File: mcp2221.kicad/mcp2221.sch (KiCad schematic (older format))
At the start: 17 parts, among them J2 Jumper 32 or 21, J3 Conn_01x04_Male, J4 Conn_01x07_Male, J5 Conn_01x02_Male, J6 Conn_01x02_Male, U1 AMS1117CD-3.3, U2 MCP2221

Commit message: replaced 4-pin USB-connector with 5-pin connector
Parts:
- removed USB1: Conn_01x04, symbol Connector_Generic:Conn_01x04
- added USB1: Micro-USB_Breakout, symbol User:Micro-USB_Breakout
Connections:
- wire segments 37 -> 41
- no-connect marks 0 -> 1
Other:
- note removed: "VBUS\nD+\nD-\nGND"
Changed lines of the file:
@@
 Sheet 1 1
 Title "MCP2221 Breakout"
-Date "2020-03-06"
-Rev "2"
+Date "2020-03-10"
+Rev "3"
 Comp "https://github.com/bablokb/pcb-mcp2221"
 Comment1 ""
@@
 L power:GND #PWR0102
 U 1 1 5E4BC7DA
-P 2300 2500
-F 0 "#PWR0102" H 2300 2250 50  0001 C CNN
-F 1 "GND" H 2305 2327 50  0000 C CNN
-F 2 "" H 2300 2500 50  0001 C CNN
-F 3 "" H 2300 2500 50  0001 C CNN
-	1    2300 2500
+P 3050 2600
+F 0 "#PWR0102" H 3050 2350 50  0001 C CNN
+F 1 "GND" H 3055 2427 50  0000 C CNN
+F 2 "" H 3050 2600 50  0001 C CNN
+F 3 "" H 3050 2600 50  0001 C CNN
+	1    3050 2600
 	1    0    0    -1
 $EndComp
@@
 	4200 2600 4200 2800
 Connection ~ 4200 2800
-$Comp
-L Connector_Generic:Conn_01x04 USB1
-U 1 1 5E611DD7
-P 2100 2400
-F 0 "USB1" H 2018 1975 50  0000 C CNN
-F 1 "Conn_01x04" H 2018 2066 50  0000 C CNN
-F 2 "" H 2100 2400 50  0001 C CNN
-F 3 "~" H 2100 2400 50  0001 C CNN
-	1    2100 2400
-	-1   0    0    1
-$EndComp
-Text Notes 2000 2500 2    50   ~ 0
-VBUS\nD+\nD-\nGND
-$Comp
-L power:PWR_FLAG #FLG0102
-U 1 1 5E615FD4
-P 2300 2500
-F 0 "#FLG0102" H 2300 2575 50  0001 C CNN
-F 1 "PWR_FLAG" V 2300 2627 50  0000 L CNN
-F 2 "" H 2300 2500 50  0001 C CNN
-F 3 "~" H 2300 2500 50  0001 C CNN
-	1    2300 2500
-	0    1    1    0
-$EndComp
-Connection ~ 2300 2500
 Wire Wire Line
 	2300 2200 2300 1800
@@
 Wire Wire Line
 	3500 2200 3500 2100
-Connection ~ 2300 2200
 $Comp
 L power:PWR_FLAG #FLG0103
@@
 Wire Wire Line
 	4000 2450 3850 2450
-$Comp
-L power:GND #PWR0106
-U 1 1 5E625316
-P 3550 2450
-F 0 "#PWR0106" H 3550 2200 50  0001 C CNN
-F 1 "GND" V 3555 2322 50  0000 R CNN
-F 2 "" H 3550 2450 50  0001 C CNN
-F 3 "" H 3550 2450 50  0001 C CNN
-	1    3550 2450
-	0    1    1    0
-$EndComp
 Connection ~ 3850 1450
 Wire Wire Line
@@
 Text Label 7250 1950 0    50   ~ 0
 ~RST~
+$Comp
+L User:Micro-USB_Breakout USB1
+U 1 1 5E68A411
+P 2100 2400
+F 0 "USB1" H 2100 2750 50  0000 C CNN
+F 1 "Micro-USB_Breakout" H 2100 2850 50  0000 C CNN
+F 2 "" H 2100 2400 50  0001 C CNN
+F 3 "~" H 2100 2400 50  0001 C CNN
+	1    2100 2400
+	-1   0    0    1
+$EndComp
+Connection ~ 2300 2200
+NoConn ~ 2300 2500
+Wire Wire Line
+	2300 2600 2750 2600
+Wire Wire Line
+	3550 2450 3050 2450
+Wire Wire Line
+	3050 2450 3050 2600
+Connection ~ 3050 2600
+$Comp
+L power:PWR_FLAG #FLG0102
+U 1 1 5E691293
+P 2750 2600
+F 0 "#FLG0102" H 2750 2675 50  0001 C CNN
+F 1 "PWR_FLAG" H 2550 2550 50  0000 L CNN
+F 2 "" H 2750 2600 50  0001 C CNN
+F 3 "~" H 2750 2600 50  0001 C CNN
+	1    2750 2600
+	-1   0    0    1
+$EndComp
+Connection ~ 2750 2600
+Wire Wire Line
+	2750 2600 3050 2600
+Text Label 5500 2300 0    50   ~ 0
+~RST~
 $EndSCHEMATC

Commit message: Rev 4: added pullups for all GPs, added SW1 to GP3
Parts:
- added J3, J4: Conn_01x02_Male, symbol Connector:Conn_01x02_Male
- added R4, R6: 2.2K, symbol Device:R
- added R5, R7: 2.2k, symbol Device:R
- added SW1: SW_Push, symbol Switch:SW_Push
- J6: renamed from J5; value Conn_01x02_Male -> Conn_01x03_Male; symbol Connector:Conn_01x02_Male -> Connector:Conn_01x03_Male
- J7: renamed from J6; value Conn_01x02_Male -> Conn_01x03_Male; symbol Connector:Conn_01x02_Male -> Connector:Conn_01x03_Male
- renumbered J4 to J1, J3 to J5, R5 to R1, R1 to R2, R2 to R3, R3 to R8, R4 to R9
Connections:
- net GND: now also SW1.2
- net GP0: now also J6.2 (Pin_2); no longer J6.1 (Pin_1)
- net GP2: now also J3.1 (Pin_1)
- net GP3: now also J4.2 (Pin_2), SW1.1
- net VDD: now reaches C2.1, J2.2 (Pin_2), J5.2 (Pin_2), R1.2, R2.1, R3.1, U2.1 (VDD)
- net VDD: now also R4.1, R5.2, R6.1, R7.2
- net at R8.1: now also J6.3 (Pin_3); no longer J6.2 (Pin_2)
- new net: J6.1 (Pin_1), R6.2
- new net: J7.3 (Pin_3), R7.1
- new net: J3.2 (Pin_2), R4.2
- new net: J4.1 (Pin_1), R5.1
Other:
- moved on the sheet: D1, D2, J1, R1, R8, R9

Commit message: added footprints, created initial pcb
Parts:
- C1, C2: footprint (none) -> Capacitor_THT:C_Disc_D4.3mm_W1.9mm_P5.00mm
- D1, D2: footprint (none) -> LED_THT:LED_Rectangular_W3.0mm_H2.0mm
- J1: footprint (none) -> Connector_PinHeader_2.54mm:PinHeader_1x07_P2.54mm_Vertical
- J2, J6, J7: footprint (none) -> Connector_PinHeader_2.54mm:PinHeader_1x03_P2.54mm_Vertical
- J3, J4: footprint (none) -> Connector_PinHeader_2.54mm:PinHeader_1x02_P2.54mm_Vertical
- J5: footprint (none) -> Connector_PinHeader_2.54mm:PinHeader_1x04_P2.54mm_Vertical
- R1, R2, R3, R4, R5, R6, R7, R8, R9: footprint (none) -> Resistor_THT:R_Axial_DIN0204_L3.6mm_D1.6mm_P7.62mm_Horizontal
- SW1: footprint (none) -> Button_Switch_THT:SW_DIP_SPSTx01_Piano_10.8x4.1mm_W7.62mm_P2.54mm
- U1: footprint Package_TO_SOT_SMD:TO-252-3_TabPin2 -> user:AMS1117_Breakout
- USB1: footprint (none) -> user:Micro-USB_Breakout
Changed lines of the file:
@@
 F 0 "U1" H 3150 1692 50  0000 C CNN
 F 1 "AMS1117CD-3.3" H 3150 1601 50  0000 C CNN
-F 2 "Package_TO_SOT_SMD:TO-252-3_TabPin2" H 3150 1650 50  0001 C CNN
+F 2 "user:AMS1117_Breakout" H 3150 1650 50  0001 C CNN
 F 3 "http://www.advanced-monolithic.com/pdf/ds1117.pdf" H 3250 1200 50  0001 C CNN
 	1    3150 1450
@@
 F 0 "J5" H 5072 3482 50  0000 R CNN
 F 1 "Conn_01x04_Male" H 5072 3573 50  0000 R CNN
-F 2 "" H 5100 3600 50  0001 C CNN
+F 2 "Connector_PinHeader_2.54mm:PinHeader_1x04_P2.54mm_Vertical" H 5100 3600 50  0001 C CNN
 F 3 "~" H 5100 3600 50  0001 C CNN
 	1    5100 3600
@@
 F 0 "R2" H 4270 3196 50  0000 L CNN
 F 1 "2.2k" H 4270 3105 50  0000 L CNN
-F 2 "" V 4130 3150 50  0001 C CNN
+F 2 "Resistor_THT:R_Axial_DIN0204_L3.6mm_D1.6mm_P7.62mm_Horizontal" V 4130 3150 50  0001 C CNN
 F 3 "~" H 4200 3150 50  0001 C CNN
 	1    4200 3150
@@
 F 0 "R3" H 4520 3196 50  0000 L CNN
 F 1 "2.2K" H 4520 3105 50  0000 L CNN
-F 2 "" V 4380 3150 50  0001 C CNN
+F 2 "Resistor_THT:R_Axial_DIN0204_L3.6mm_D1.6mm_P7.62mm_Horizontal" V 4380 3150 50  0001 C CNN
 F 3 "~" H 4450 3150 50  0001 C CNN
 	1    4450 3150
@@
 F 0 "R8" H 6450 4100 50  0000 L CNN
 F 1 "1K" H 6450 4000 50  0000 L CNN
-F 2 "" V 6580 4050 50  0001 C CNN
+F 2 "Resistor_THT:R_Axial_DIN0204_L3.6mm_D1.6mm_P7.62mm_Horizontal" V 6580 4050 50  0001 C CNN
 F 3 "~" H 6650 4050 50  0001 C CNN
 	1    6650 4050
@@
 F 0 "R9" H 6970 4096 50  0000 L CNN
 F 1 "1K" H 6970 4005 50  0000 L CNN
-F 2 "" V 6830 4050 50  0001 C CNN
+F 2 "Resistor_THT:R_Axial_DIN0204_L3.6mm_D1.6mm_P7.62mm_Horizontal" V 6830 4050 50  0001 C CNN
 F 3 "~" H 6900 4050 50  0001 C CNN
 	1    6900 4050
@@
 F 0 "D1" V 6700 4550 50  0000 R CNN
 F 1 "LED" V 6600 4600 50  0000 R CNN
-F 2 "" H 6650 4350 50  0001 C CNN
+F 2 "LED_THT:LED_Rectangular_W3.0mm_H2.0mm" H 6650 4350 50  0001 C CNN
 F 3 "~" H 6650 4350 50  0001 C CNN
 	1    6650 4350
@@
 F 0 "D2" V 6939 4233 50  0000 R CNN
 F 1 "LED" V 6848 4233 50  0000 R CNN
-F 2 "" H 6900 4350 50  0001 C CNN
+F 2 "LED_THT:LED_Rectangular_W3.0mm_H2.0mm" H 6900 4350 50  0001 C CNN
 F 3 "~" H 6900 4350 50  0001 C CNN
 	1    6900 4350
@@
 F 0 "J6" H 6300 3800 50  0000 C CNN
 F 1 "Conn_01x03_Male" H 6100 3700 50  0000 C CNN
-F 2 "" H 6450 3800 50  0001 C CNN
+F 2 "Connector_PinHeader_2.54mm:PinHeader_1x03_P2.54mm_Vertical" H 6450 3800 50  0001 C CNN
 F 3 "~" H 6450 3800 50  0001 C CNN
 	1    6450 3800
@@
 F 0 "J7" H 7072 3682 50  0000 R CNN
 F 1 "Conn_01x03_Male" H 7072 3773 50  0000 R CNN
-F 2 "" H 7100 3800 50  0001 C CNN
+F 2 "Connector_PinHeader_2.54mm:PinHeader_1x03_P2.54mm_Vertical" H 7100 3800 50  0001 C CNN
 F 3 "~" H 7100 3800 50  0001 C CNN
 	1    7100 3800
@@
 F 0 "C1" H 3600 1000 50  0000 C CNN
 F 1 "0.47µF" H 3550 1100 50  0000 C CNN
-F 2 "" H 3888 900 50  0001 C CNN
+F 2 "Capacitor_THT:C_Disc_D4.3mm_W1.9mm_P5.00mm" H 3888 900 50  0001 C CNN
 F 3 "~" H 3850 1050 50  0001 C CNN
 	1    3850 1050
@@
 F 0 "J2" V 3662 2044 50  0000 L CNN
 F 1 "Jumper 32 or 21" V 3550 1700 50  0000 L CNN
-F 2 "" H 3600 1900 50  0001 C CNN
+F 2 "Connector_PinHeader_2.54mm:PinHeader_1x03_P2.54mm_Vertical" H 3600 1900 50  0001 C CNN
 F 3 "~" H 3600 1900 50  0001 C CNN
 	1    3600 1900
@@
 F 0 "R1" H 5570 2596 50  0000 L CNN
 F 1 "10K" H 5570 2505 50  0000 L CNN
-F 2 "" V 5430 2550 50  0001 C CNN
+F 2 "Resistor_THT:R_Axial_DIN0204_L3.6mm_D1.6mm_P7.62mm_Horizontal" V 5430 2550 50  0001 C CNN
 F 3 "~" H 5500 2550 50  0001 C CNN
 	1    5500 2550
@@
 F 0 "C2" V 3850 2450 50  0000 C CNN
 F 1 "0.1 µF" V 3950 2450 50  0000 C CNN
-F 2 "" H 3738 2300 50  0001 C CNN
+F 2 "Capacitor_THT:C_Disc_D4.3mm_W1.9mm_P5.00mm" H 3738 2300 50  0001 C CNN
 F 3 "~" H 3700 2450 50  0001 C CNN
 	1    3700 2450
@@
 F 0 "USB1" H 2100 2750 50  0000 C CNN
 F 1 "Micro-USB_Breakout" H 2100 2850 50  0000 C CNN
-F 2 "" H 2100 2400 50  0001 C CNN
+F 2 "user:Micro-USB_Breakout" H 2100 2400 50  0001 C CNN
 F 3 "~" H 2100 2400 50  0001 C CNN
 	1    2100 2400
@@
 F 0 "R6" H 6570 3496 50  0000 L CNN
 F 1 "2.2K" H 6570 3405 50  0000 L CNN
-F 2 "" V 6430 3450 50  0001 C CNN
+F 2 "Resistor_THT:R_Axial_DIN0204_L3.6mm_D1.6mm_P7.62mm_Horizontal" V 6430 3450 50  0001 C CNN
 F 3 "~" H 6500 3450 50  0001 C CNN
 	1    6500 3450
@@
 F 0 "R7" H 7120 3496 50  0000 L CNN
 F 1 "2.2k" H 7120 3405 50  0000 L CNN
-F 2 "" V 6980 3450 50  0001 C CNN
+F 2 "Resistor_THT:R_Axial_DIN0204_L3.6mm_D1.6mm_P7.62mm_Horizontal" V 6980 3450 50  0001 C CNN
 F 3 "~" H 7050 3450 50  0001 C CNN
 	1    7050 3450
@@
 F 0 "R4" H 8470 3446 50  0000 L CNN
 F 1 "2.2K" H 8470 3355 50  0000 L CNN
-F 2 "" V 8330 3400 50  0001 C CNN
+F 2 "Resistor_THT:R_Axial_DIN0204_L3.6mm_D1.6mm_P7.62mm_Horizontal" V 8330 3400 50  0001 C CNN
 F 3 "~" H 8400 3400 50  0001 C CNN
 	1    8400 3400
@@
 F 0 "R5" H 9020 3446 50  0000 L CNN
 F 1 "2.2k" H 9020 3355 50  0000 L CNN
-F 2 "" V 8880 3400 50  0001 C CNN
+F 2 "Resistor_THT:R_Axial_DIN0204_L3.6mm_D1.6mm_P7.62mm_Horizontal" V 8880 3400 50  0001 C CNN
 F 3 "~" H 8950 3400 50  0001 C CNN
 	1    8950 3400
@@
 F 0 "J3" H 8250 2950 50  0000 C CNN
 F 1 "Conn_01x02_Male" H 7950 2850 50  0000 C CNN
-F 2 "" H 8350 2950 50  0001 C CNN
+F 2 "Connector_PinHeader_2.54mm:PinHeader_1x02_P2.54mm_Vertical" H 8350 2950 50  0001 C CNN
 F 3 "~" H 8350 2950 50  0001 C CNN
 	1    8350 2950
@@
 F 0 "J4" H 8972 2932 50  0000 R CNN
 F 1 "Conn_01x02_Male" H 8972 3023 50  0000 R CNN
-F 2 "" H 9000 3050 50  0001 C CNN
+F 2 "Connector_PinHeader_2.54mm:PinHeader_1x02_P2.54mm_Vertical" H 9000 3050 50  0001 C CNN
 F 3 "~" H 9000 3050 50  0001 C CNN
 	1    9000 3050
@@
 F 0 "J1" V 7600 1750 50  0000 C CNN
 F 1 "Conn_01x07_Male" V 7450 1800 50  0000 C CNN
-F 2 "" H 7000 1750 50  0001 C CNN
+F 2 "Connector_PinHeader_2.54mm:PinHeader_1x07_P2.54mm_Vertical" H 7000 1750 50  0001 C CNN
 F 3 "~" H 7000 1750 50  0001 C CNN
 	1    7000 1750
@@
 F 0 "SW1" H 8150 2535 50  0000 C CNN
 F 1 "SW_Push" H 8150 2444 50  0000 C CNN
-F 2 "" H 8150 2450 50  0001 C CNN
+F 2 "Button_Switch_THT:SW_DIP_SPSTx01_Piano_10.8x4.1mm_W7.62mm_P2.54mm" H 8150 2450 50  0001 C CNN
 F 3 "~" H 8150 2450 50  0001 C CNN
 	1    8150 2250
@@
 	7950 2500 8800 2500
 $Comp
-L power:GND #PWR?
+L power:GND #PWR0101
 U 1 1 5E6B663C
 P 8550 2250
-F 0 "#PWR?" H 8550 2000 50  0001 C CNN
+F 0 "#PWR0101" H 8550 2000 50  0001 C CNN
 F 1 "GND" H 8555 2077 50  0000 C CNN
 F 2 "" H 8550 2250 50  0001 C CNN

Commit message: Rev 6: switched to SMD, added connector, minor tweaks
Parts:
- added J6: Conn_01x06_Male, Connector_PinHeader_2.54mm:PinHeader_1x06_P2.54mm_Vertical, symbol Connector:Conn_01x06_Male
- C1: renamed from C2; footprint Capacitor_THT:C_Disc_D4.3mm_W1.9mm_P5.00mm -> Capacitor_SMD:C_1206_3216Metric_Pad1.42x1.75mm_HandSolder
- C2: renamed from C1; footprint Capacitor_THT:C_Disc_D4.3mm_W1.9mm_P5.00mm -> Capacitor_SMD:C_1206_3216Metric_Pad1.42x1.75mm_HandSolder
- D1, D2: footprint LED_THT:LED_Rectangular_W3.0mm_H2.0mm -> LED_SMD:LED_1206_3216Metric_Pad1.42x1.75mm_HandSolder
- J4: renamed from J1; value Conn_01x07_Male -> Conn_01x06_Male; footprint Connector_PinHeader_2.54mm:PinHeader_1x07_P2.54mm_Vertical -> Connector_PinHeader_2.54mm:PinHeader_1x06_P2.54mm_Vertical; symbol Connector:Conn_01x07_Male -> Connector:Conn_01x06_Male
- R1: renamed from R2; footprint Resistor_THT:R_Axial_DIN0204_L3.6mm_D1.6mm_P7.62mm_Horizontal -> Resistor_SMD:R_1206_3216Metric_Pad1.42x1.75mm_HandSolder
- R2: renamed from R3; footprint Resistor_THT:R_Axial_DIN0204_L3.6mm_D1.6mm_P7.62mm_Horizontal -> Resistor_SMD:R_1206_3216Metric_Pad1.42x1.75mm_HandSolder
- R3: renamed from R1; footprint Resistor_THT:R_Axial_DIN0204_L3.6mm_D1.6mm_P7.62mm_Horizontal -> Resistor_SMD:R_1206_3216Metric_Pad1.42x1.75mm_HandSolder
- R4: renamed from R6; value 2.2K -> 4.7K; footprint Resistor_THT:R_Axial_DIN0204_L3.6mm_D1.6mm_P7.62mm_Horizontal -> Resistor_SMD:R_1206_3216Metric_Pad1.42x1.75mm_HandSolder
- R5: renamed from R8; footprint Resistor_THT:R_Axial_DIN0204_L3.6mm_D1.6mm_P7.62mm_Horizontal -> Resistor_SMD:R_1206_3216Metric_Pad1.42x1.75mm_HandSolder
- R6: renamed from R9; footprint Resistor_THT:R_Axial_DIN0204_L3.6mm_D1.6mm_P7.62mm_Horizontal -> Resistor_SMD:R_1206_3216Metric_Pad1.42x1.75mm_HandSolder
- R7: value 2.2k -> 4.7K; footprint Resistor_THT:R_Axial_DIN0204_L3.6mm_D1.6mm_P7.62mm_Horizontal -> Resistor_SMD:R_1206_3216Metric_Pad1.42x1.75mm_HandSolder
- R8: renamed from R4; value 2.2K -> 4.7K; footprint Resistor_THT:R_Axial_DIN0204_L3.6mm_D1.6mm_P7.62mm_Horizontal -> Resistor_SMD:R_1206_3216Metric_Pad1.42x1.75mm_HandSolder
- R9: renamed from R5; value 2.2k -> 4.7K; footprint Resistor_THT:R_Axial_DIN0204_L3.6mm_D1.6mm_P7.62mm_Horizontal -> Resistor_SMD:R_1206_3216Metric_Pad1.42x1.75mm_HandSolder
- SW1: footprint Button_Switch_THT:SW_DIP_SPSTx01_Piano_10.8x4.1mm_W7.62mm_P2.54mm -> Button_Switch_SMD:SW_Push_1P1T_NO_6x6mm_H9.5mm
- renumbered J2 to J1, J5 to J2, J6 to J3, J7 to J5, J3 to J7, J4 to J8
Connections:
- net GND: now also J6.5 (Pin_5)
- net GP3: now also J8.1 (Pin_1); no longer J8.2 (Pin_2)
- net SCL: now also J6.2 (Pin_2)
- net SDA: now also J6.1 (Pin_1)
- net ~RST~: now also J6.3 (Pin_3); no longer J4.7 (Pin_7)
- net 3.3V: now reaches C2.1, J1.1 (Pin_1), U1.2 (VO), U2.11 (VUSB)
- net 3.3V: now also J6.4 (Pin_4)
- net 5V: now reaches J1.3 (Pin_3), U1.3 (VI), USB1.5 (Pin_5)
- net 5V: now also J6.6 (Pin_6)
- net at R6.1: now also J5.3 (Pin_3); no longer J5.1 (Pin_1)
- net at R7.1: now also J5.1 (Pin_1); no longer J5.3 (Pin_3)
- net at R9.1: now also J8.2 (Pin_2); no longer J8.1 (Pin_1)

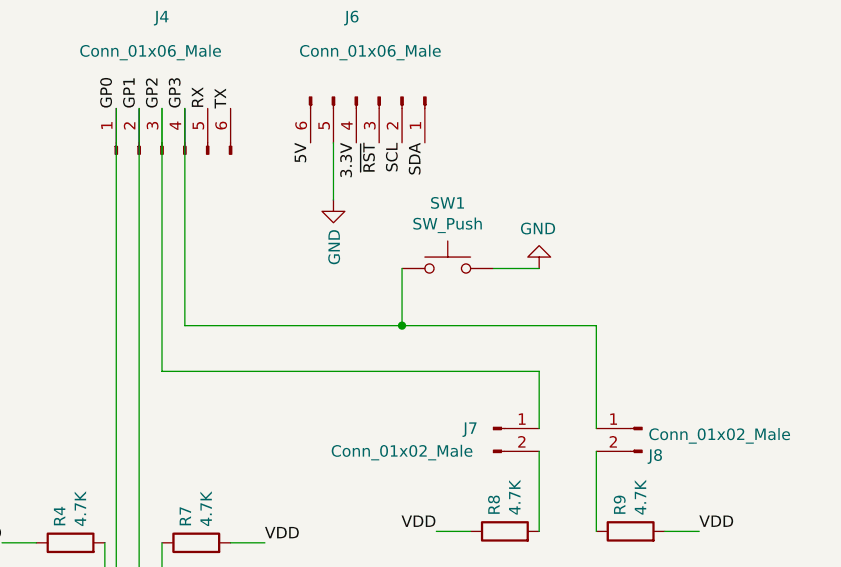
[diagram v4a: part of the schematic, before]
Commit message: Rev 7: added button for GP2
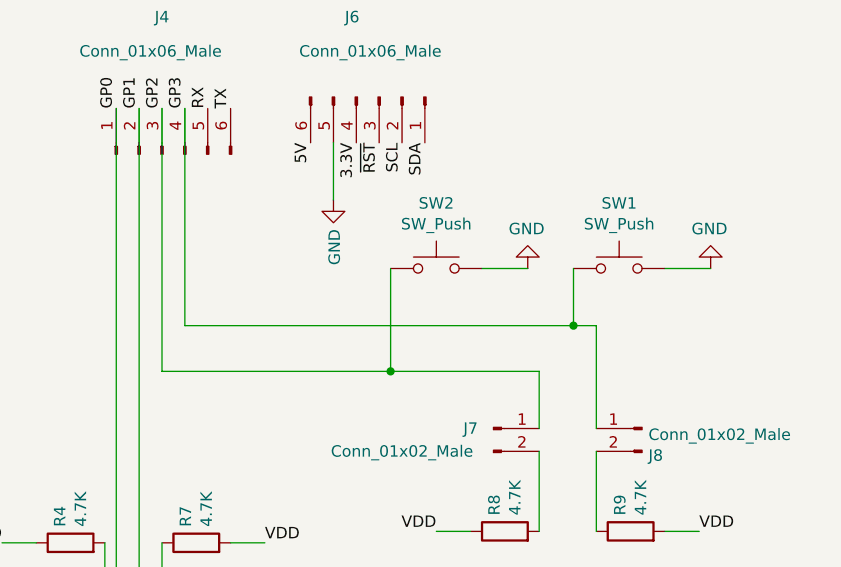
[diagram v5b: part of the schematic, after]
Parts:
- added SW2: SW_Push, Button_Switch_SMD:SW_Push_1P1T_NO_6x6mm_H9.5mm, symbol Switch:SW_Push
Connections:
- net GND: now also SW2.2
- net GP2: now also SW2.1
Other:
- moved on the sheet: SW1
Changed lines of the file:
@@
 Sheet 1 1
 Title "MCP2221 Breakout"
-Date "2020-04-09"
-Rev "6"
+Date "2020-04-14"
+Rev "7"
 Comp "https://github.com/bablokb/pcb-mcp2221"
 Comment1 ""
@@
 	8550 3050 8550 3400
 Wire Wire Line
-	6900 2700 8550 2700
+	6900 2700 7900 2700
 Wire Wire Line
 	8550 2700 8550 2950
-Wire Wire Line
-	7000 2500 7950 2500
 Wire Wire Line
 	8800 2500 8800 2950
@@
 L Switch:SW_Push SW1
 U 1 1 5E6B4B53
-P 8150 2250
-F 0 "SW1" H 8150 2535 50  0000 C CNN
-F 1 "SW_Push" H 8150 2444 50  0000 C CNN
-F 2 "Button_Switch_SMD:SW_Push_1P1T_NO_6x6mm_H9.5mm" H 8150 2450 50  0001 C CNN
-F 3 "~" H 8150 2450 50  0001 C CNN
-	1    8150 2250
-	1    0    0    -1
-$EndComp
-Wire Wire Line
-	7950 2250 7950 2500
-Connection ~ 7950 2500
-Wire Wire Line
-	7950 2500 8800 2500
+P 8900 2250
+F 0 "SW1" H 8900 2535 50  0000 C CNN
+F 1 "SW_Push" H 8900 2444 50  0000 C CNN
+F 2 "Button_Switch_SMD:SW_Push_1P1T_NO_6x6mm_H9.5mm" H 8900 2450 50  0001 C CNN
+F 3 "~" H 8900 2450 50  0001 C CNN
+	1    8900 2250
+	1    0    0    -1
+$EndComp
+Wire Wire Line
+	8700 2250 8700 2500
 $Comp
 L power:GND #PWR09
 U 1 1 5E6B663C
-P 8550 2250
-F 0 "#PWR09" H 8550 2000 50  0001 C CNN
-F 1 "GND" H 8555 2077 50  0000 C CNN
-F 2 "" H 8550 2250 50  0001 C CNN
-F 3 "" H 8550 2250 50  0001 C CNN
-	1    8550 2250
-	-1   0    0    1
-$EndComp
-Wire Wire Line
-	8350 2250 8550 2250
+P 9300 2250
+F 0 "#PWR09" H 9300 2000 50  0001 C CNN
+F 1 "GND" H 9305 2077 50  0000 C CNN
+F 2 "" H 9300 2250 50  0001 C CNN
+F 3 "" H 9300 2250 50  0001 C CNN
+	1    9300 2250
+	-1   0    0    1
+$EndComp
+Wire Wire Line
+	9100 2250 9300 2250
 $Comp
 L Connector:Conn_01x06_Male J6
@@
 Wire Wire Line
 	3850 1450 3700 1450
+Connection ~ 8700 2500
+Wire Wire Line
+	8700 2500 8800 2500
+$Comp
+L Switch:SW_Push SW2
+U 1 1 5E9641FD
+P 8100 2250
+F 0 "SW2" H 8100 2535 50  0000 C CNN
+F 1 "SW_Push" H 8100 2444 50  0000 C CNN
+F 2 "Button_Switch_SMD:SW_Push_1P1T_NO_6x6mm_H9.5mm" H 8100 2450 50  0001 C CNN
+F 3 "~" H 8100 2450 50  0001 C CNN
+	1    8100 2250
+	1    0    0    -1
+$EndComp
+$Comp
+L power:GND #PWR0101
+U 1 1 5E964208
+P 8500 2250
+F 0 "#PWR0101" H 8500 2000 50  0001 C CNN
+F 1 "GND" H 8505 2077 50  0000 C CNN
+F 2 "" H 8500 2250 50  0001 C CNN
+F 3 "" H 8500 2250 50  0001 C CNN
+	1    8500 2250
+	-1   0    0    1
+$EndComp
+Wire Wire Line
+	8300 2250 8500 2250
+Wire Wire Line
+	7000 2500 8700 2500
+Wire Wire Line
+	7900 2250 7900 2700
+Connection ~ 7900 2700
+Wire Wire Line
+	7900 2700 8550 2700
 $EndSCHEMATC
